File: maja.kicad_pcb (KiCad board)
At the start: 2 copper layers, 49 x 57.5 mm, 55 parts, among them J1 USB, K1 CONN_3, P1 JTAG, P2 CONN_8, SW1 RESET, SW2 BTN, SW3 BTN, U1 CC2538, U2 TPS70933, U3 Antenna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

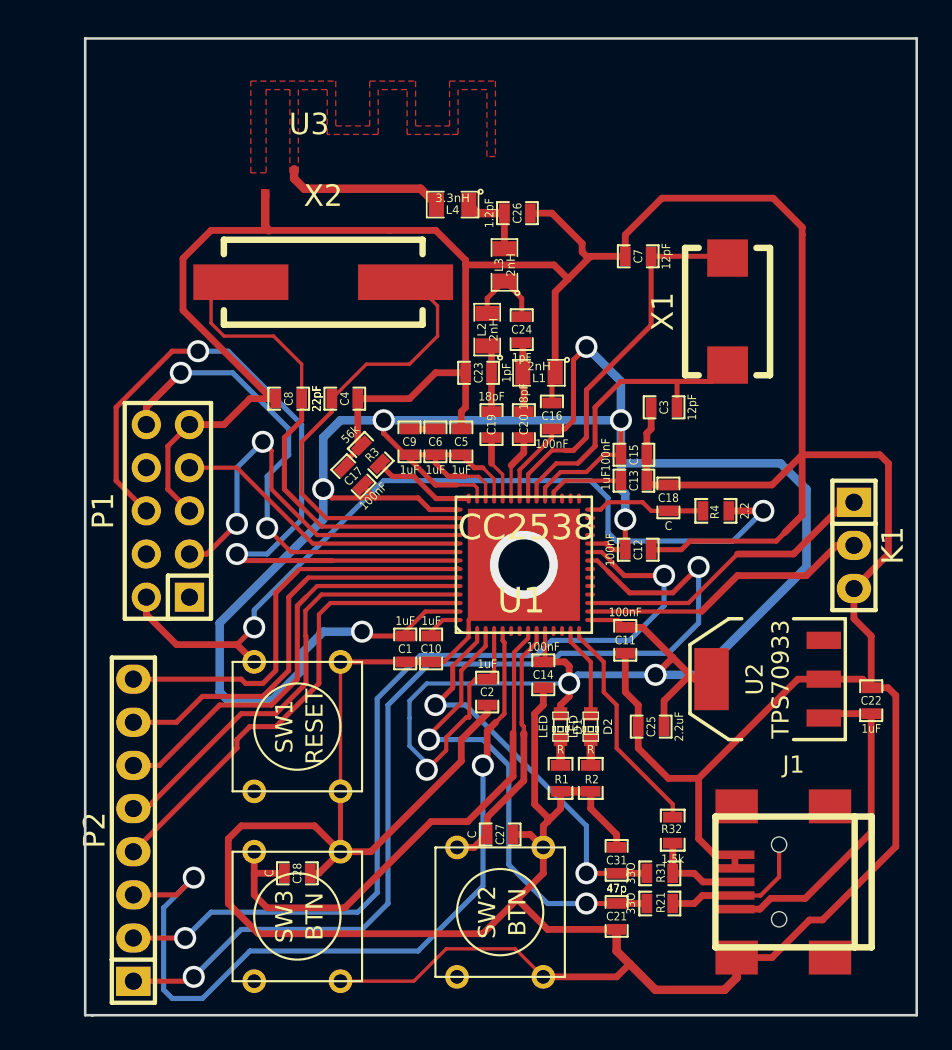
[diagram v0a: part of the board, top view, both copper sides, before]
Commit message: Added copper fills, changed net tie so that antenna now looks okay
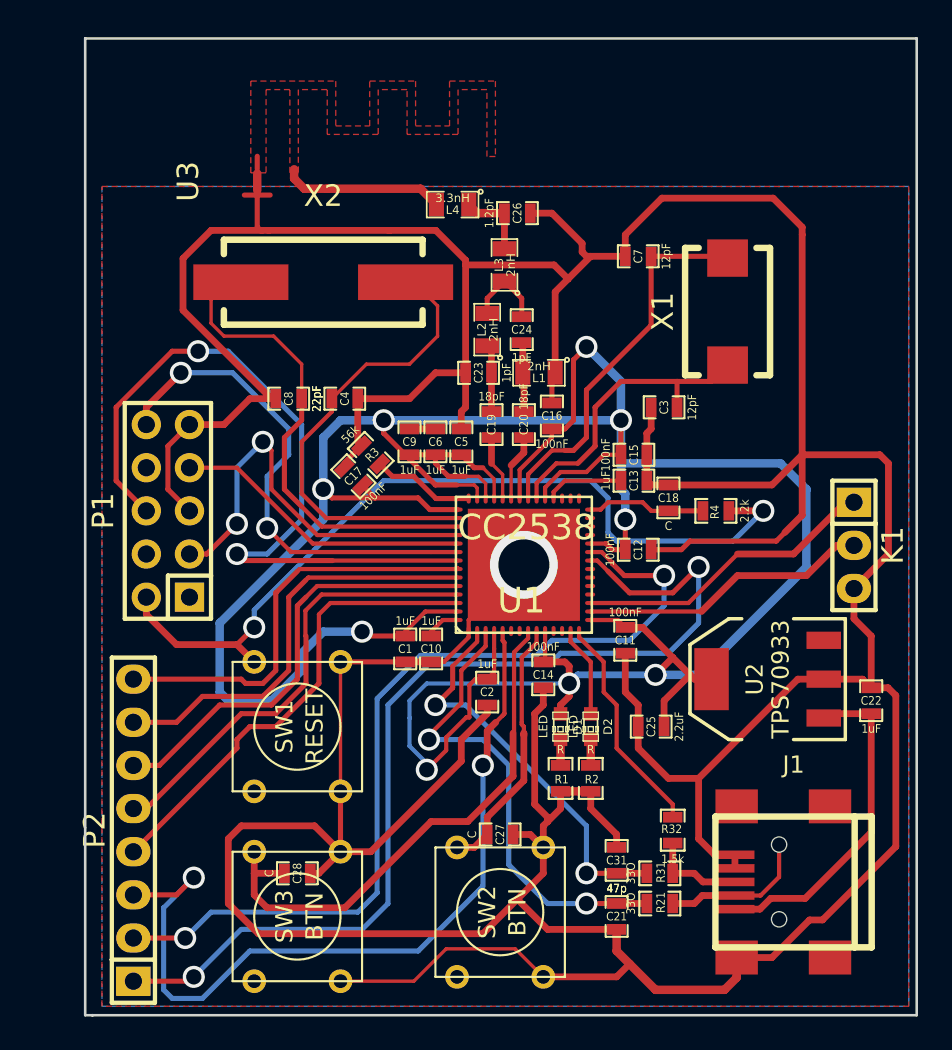
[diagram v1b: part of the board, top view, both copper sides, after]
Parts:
- R4: value 2.2 -> 2.2k
- U3: footprint Oddities:NetTie-I_SMD -> Oddities:NetTie-I_Connected_SMD
- moved U3 3.08 mm to (76.4, 79.7), turned to 270 degrees
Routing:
- net GND: track 346.3 -> 347.9 mm
- net Net-(L4-Pad2): track 9.56 -> 10.3 mm
- added copper zone on B.Cu, net GND
- added copper zone on F.Cu, net GND
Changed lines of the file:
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@@
   (general
     (links 130)
-    (no_connects 4)
+    (no_connects 3)
     (area 66.174999 71.174999 115.275001 128.825001)
     (thickness 1.6)
     (drawings 33)
-    (tracks 612)
+    (tracks 619)
     (zones 0)
     (modules 55)
@@
     (user_trace_width 0.5)
     (trace_clearance 0.2)
-    (zone_clearance 0.508)
+    (zone_clearance 0)
     (zone_45_only yes)
     (trace_min 0.2)
@@
     (mod_text_size 1.5 1.5)
     (mod_text_width 0.15)
-    (pad_size 0.5 0.5)
+    (pad_size 0.1 0.1)
     (pad_drill 0)
     (pad_to_mask_clearance 0.2)
@@
     (add_net VDD)
   )
+  (module Oddities:NetTie-I_Connected_SMD (layer F.Cu)
+    (at 76.38 79.708 270)
+    (descr "Just a \"Net tie\" as an more or less elegant way to connect two different nets without disturbing ERC and DRC.")
+    (tags "Just a \"Net tie\" as an more or less elegant way to connect two different nets without disturbing ERC and DRC.")
+    (fp_text reference U3 (at -0.04064 4.06908 270) (layer F.SilkS)
+      (effects (font (size 1.27 1.27) (thickness 0.254)))
+    )
+    (fp_text value Antenna (at 0 -3.048 270) (layer F.SilkS) hide
+      (effects (font (size 1.27 1.27) (thickness 0.254)))
+    )
+    (fp_line (start 0.492 0) (end -0.508 0) (layer F.Cu) (width 0.5))
+    (pad 1 smd rect (at -0.762 0 270) (size 0.1 0.1) (layers F.Cu F.Paste F.Mask)
+      (net 35 "Net-(L4-Pad2)"))
+    (pad 2 smd rect (at 0.762 0 270) (size 0.1 0.1) (layers F.Cu F.Paste F.Mask)
+      (net 19 GND))
+  )
   (module STUB (layer F.Cu)
     (at 0 0)
@@
       (effects (font (size 0.50038 0.4572) (thickness 0.1143)))
     )
-    (fp_text value 2.2 (at -1.69926 0 270) (layer F.SilkS)
+    (fp_text value 2.2k (at -1.69926 0 270) (layer F.SilkS)
       (effects (font (size 0.508 0.4572) (thickness 0.1143)))
     )
@@
       (rotate (xyz 0 0 0))
     )
-  )
-  (module Oddities:NetTie-I_SMD (layer F.Cu)
-    (at 79.39 80.37 180)
-    (descr "Just a \"Net tie\" as an more or less elegant way to connect two different nets without disturbing ERC and DRC. Make connection between 1 and 2 by yourself.")
-    (tags "Just a \"Net tie\" as an more or less elegant way to connect two different nets without disturbing ERC and DRC. Make connection between 1 and 2 by yourself.")
-    (fp_text reference U3 (at -0.04064 4.06908 180) (layer F.SilkS)
-      (effects (font (size 1.27 1.27) (thickness 0.254)))
-    )
-    (fp_text value Antenna (at 0 -3.048 180) (layer F.SilkS) hide
-      (effects (font (size 1.27 1.27) (thickness 0.254)))
-    )
-    (pad 1 smd rect (at -1.105 0.274 180) (size 0.5 0.5) (layers F.Cu F.Paste F.Mask)
-      (net 35 "Net-(L4-Pad2)"))
-    (pad 2 smd rect (at 2.54 0 180) (size 0.5 0.5) (layers F.Cu F.Paste F.Mask)
-      (net 19 GND))
   )
   (module Connect:USB_MINI_B (layer F.Cu)
@@
   (segment (start 75.184 106.934) (end 76.2 107.95) (width 0.4) (layer F.Cu) (net 18) (status 20))
   (segment (start 71.628 106.934) (end 75.184 106.934) (width 0.4) (layer F.Cu) (net 18))
+  (segment (start 76.38 80.47) (end 75.618 80.47) (width 0.3) (layer F.Cu) (net 19))
+  (segment (start 76.38 80.47) (end 77.142 80.47) (width 0.3) (layer F.Cu) (net 19))
+  (segment (start 76.38 80.47) (end 76.38 82.354) (width 0.3) (layer F.Cu) (net 19))
+  (segment (start 76.38 82.354) (end 76.528 82.502) (width 0.3) (layer F.Cu) (net 19))
+  (segment (start 76.634 82.502) (end 76.634 82.55) (width 0.3) (layer F.Cu) (net 19))
+  (segment (start 76.528 82.502) (end 76.634 82.502) (width 0.3) (layer F.Cu) (net 19))
+  (segment (start 76.48 82.55) (end 76.528 82.502) (width 0.3) (layer F.Cu) (net 19))
   (segment (start 108.458 82.804) (end 108.458 82.358) (width 0.4) (layer F.Cu) (net 19))
   (segment (start 108.458 95.758) (end 108.458 82.804) (width 0.4) (layer F.Cu) (net 19))
@@
   (segment (start 106.75 80.65) (end 100.2 80.65) (width 0.4) (layer F.Cu) (net 19))
   (segment (start 108.458 82.358) (end 106.75 80.65) (width 0.4) (layer F.Cu) (net 19))
-  (segment (start 76.85 80.37) (end 76.85 82.35) (width 0.5) (layer F.Cu) (net 19))
-  (segment (start 76.85 82.35) (end 77.05 82.55) (width 0.5) (layer F.Cu) (net 19))
   (segment (start 84.12 82.55) (end 86.89 82.55) (width 0.4) (layer F.Cu) (net 19))
   (segment (start 86.89 82.55) (end 88.646 84.306) (width 0.4) (layer F.Cu) (net 19))
@@
   (segment (start 72.009 87.249) (end 72.009 84.201) (width 0.4) (layer F.Cu) (net 19))
   (segment (start 72.009 84.201) (end 73.66 82.55) (width 0.4) (layer F.Cu) (net 19))
-  (segment (start 73.66 82.55) (end 77.05 82.55) (width 0.4) (layer F.Cu) (net 19))
+  (segment (start 73.66 82.55) (end 76.634 82.55) (width 0.4) (layer F.Cu) (net 19))
+  (segment (start 76.634 82.55) (end 77.05 82.55) (width 0.4) (layer F.Cu) (net 19))
   (segment (start 77.05 82.55) (end 84.12 82.55) (width 0.4) (layer F.Cu) (net 19))
   (segment (start 84.12 82.55) (end 84.201 82.55) (width 0.4) (layer F.Cu) (net 19))
@@
   (segment (start 104.50068 120.904) (end 102.616 120.904) (width 0.4) (layer F.Cu) (net 34) (status 10))
   (segment (start 100.838 120.396) (end 100.838 118.618) (width 0.4) (layer F.Cu) (net 34) (status 30))
+  (segment (start 76.38 78.946) (end 76.38 78.184) (width 0.3) (layer F.Cu) (net 35))
   (segment (start 78.55 79.5) (end 78.55 78.95) (width 0.5) (layer F.Cu) (net 35))
   (segment (start 80.495 80.096) (end 79.146 80.096) (width 0.5) (layer F.Cu) (net 35))
@@
   (via (at 94.742 109.22) (size 1.3) (drill 0.9) (layers F.Cu B.Cu) (net 61))
   (zone (net 35) (net_name "Net-(L4-Pad2)") (layer F.Cu) (hatch none 0.508)
-    (connect_pads (clearance 0.508))
+    (connect_pads yes (clearance 0))
     (min_thickness 0.254)
-    (fill (arc_segments 16) (thermal_gap 0.508) (thermal_bridge_width 0.508))
+    (fill (arc_segments 16) (thermal_gap 0.5) (thermal_bridge_width 0.3))
     (polygon
       (pts
@@
       )
     )
+  )
+  (zone (net 19) (net_name GND) (layer F.Cu) (hatch edge 0.508)
+    (connect_pads (clearance 0.6))
+    (min_thickness 0.3)
+    (fill (arc_segments 16) (thermal_gap 0.508) (thermal_bridge_width 0.508))
+    (polygon
+      (pts
+        (xy 114.734 128.222) (xy 67.236 128.222) (xy 67.236 79.962) (xy 114.734 79.962) (xy 114.734 80.47)
+      )
+    )
+  )
+  (zone (net 19) (net_name GND) (layer B.Cu) (hatch edge 0.508)
+    (connect_pads (clearance 0.6))
+    (min_thickness 0.3)
+    (fill (arc_segments 16) (thermal_gap 0.508) (thermal_bridge_width 0.508))
+    (polygon
+      (pts
+        (xy 114.734 79.962) (xy 67.236 79.962) (xy 67.236 128.222) (xy 114.734 128.222) (xy 114.734 127.968)
+      )
+    )

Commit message: Add blind vias under SMD
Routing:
- net GND: track 347.9 -> 350.5 mm, vias 1 -> 28
- net /JTAG_TDI: track 44.3 -> 45.5 mm
- net /JTAG_TDO: track 29.7 -> 30.7 mm
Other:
- outline, holes or cut-outs redrawn
- rule via_min_drill: 0.508 -> 0.3
- rule via_min_size: 0.889 -> 0.3

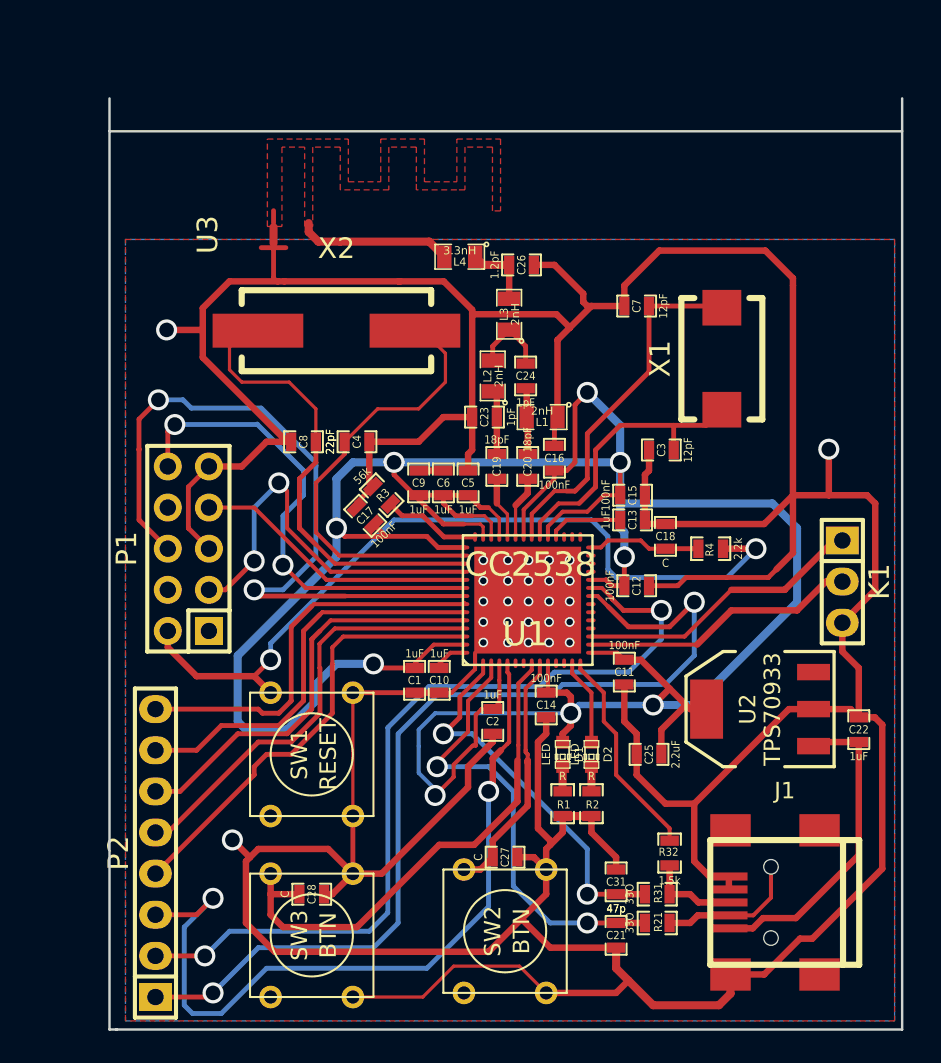
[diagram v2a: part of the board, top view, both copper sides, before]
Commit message: Resize pcb
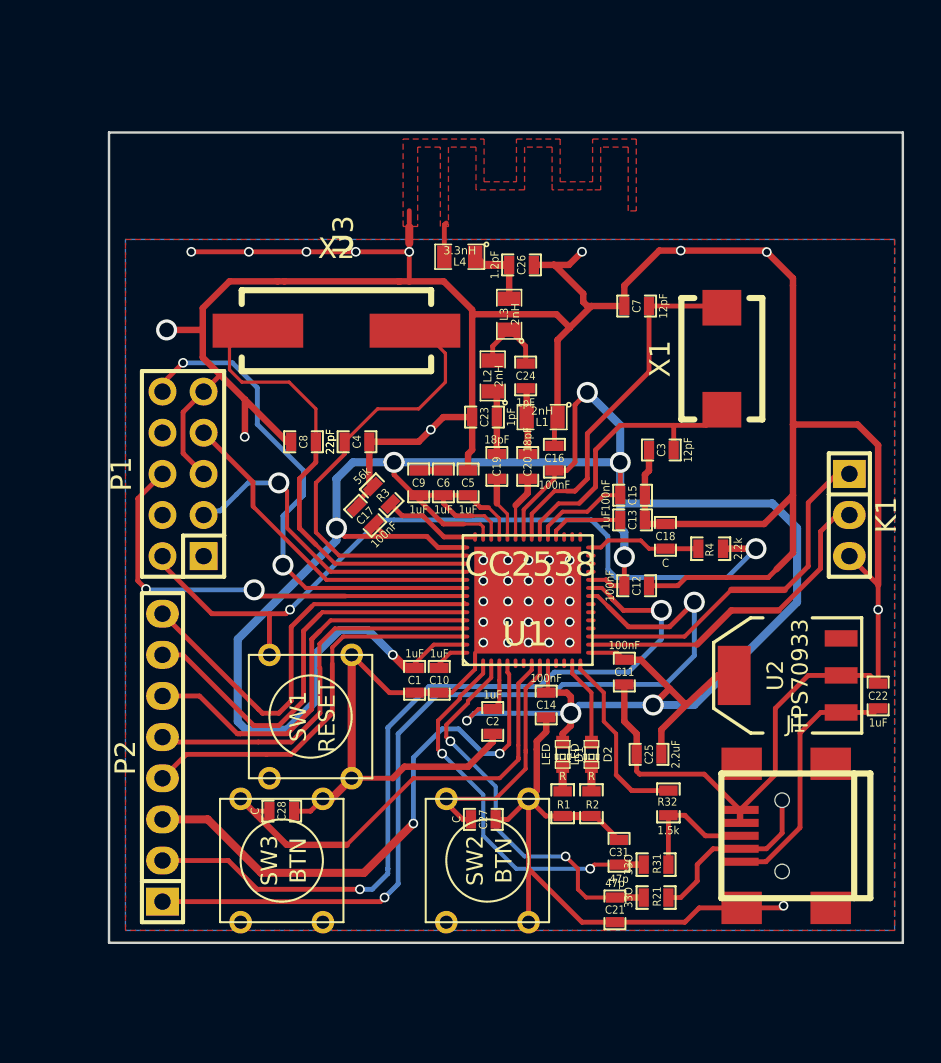
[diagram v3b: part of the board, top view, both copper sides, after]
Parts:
- moved U3 8.38 mm to (84.8, 79.7)
- moved P2 5.91 mm to (69.5, 112.0)
- moved C28 5.45 mm to (76.9, 115.3)
- moved SW3 4.98 mm to (76.9, 118.3)
- moved P1 4.63 mm to (70.8, 94.4)
- moved SW2 4.50 mm to (89.6, 118.3)
- moved J1 4.17 mm to (108.6, 116.8)
- moved K1 4.13 mm to (111.9, 97.0)
- moved R32 3.10 mm to (100.8, 114.8)
- moved C27 2.69 mm to (89.3, 115.8)
- moved U2 2.69 mm to (108.1, 106.9)
- moved C22 2.40 mm to (113.7, 108.2)
- moved SW1 2.34 mm to (78.7, 109.4)
- moved C31 1.83 mm to (97.7, 117.8)
- moved R31 1.83 mm to (100.0, 118.6)
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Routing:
- net GND: track 350.5 -> 284.4 mm, vias 28 -> 38
- net /JTAG_TDI: track 45.5 -> 27.8 mm
- net Net-(P2-Pad3): track 48.7 -> 34.8 mm
- net VDD: track 195.7 -> 187.2 mm
- net Net-(L4-Pad2): track 10.3 -> 2.90 mm
- net /BL_TX: track 18.0 -> 22.9 mm
- net Net-(P2-Pad1): track 60.0 -> 55.7 mm
- net /USB_N: track 28.0 -> 24.2 mm
- net /V_USB: track 19.8 -> 16.2 mm
- net /JTAG_TMS: track 24.1 -> 20.5 mm, vias 2 -> 1
- net /BL_RX: track 17.1 -> 20.6 mm
- net /Btn1: track 32.0 -> 28.5 mm
- net /JTAG_TCK: track 17.6 -> 20.9 mm
- net Net-(P2-Pad4): track 27.8 -> 24.7 mm
- net Net-(P2-Pad2): track 52.8 -> 50.0 mm
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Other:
- board size 49 x 57.5 mm -> 49 x 50 mm
